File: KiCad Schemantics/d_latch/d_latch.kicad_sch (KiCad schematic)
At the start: 5 parts

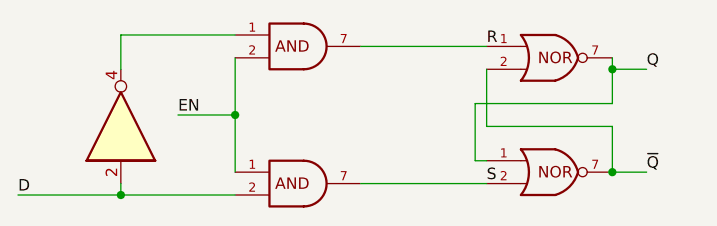
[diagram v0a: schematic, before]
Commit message: DrawIo Diagrams for the D Latch
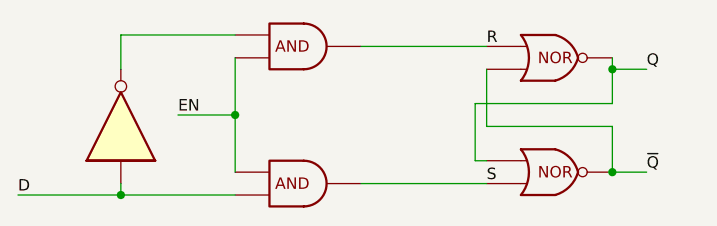
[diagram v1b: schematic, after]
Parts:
- U? (x2): value 74AUC2G08 -> (none)
- U? (x2): value 74AUC2G02 -> (none)
- U?: value 74LVC1GU04DRL -> (none); footprint Package_TO_SOT_SMD:SOT-553 -> (none)
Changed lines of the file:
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@@
     (effects (font (size 1.27 1.27)) (justify left bottom))
   )
-  (symbol (lib_id "74xGxx:74AUC2G08") (at 106.68 60.96 0) (unit 1)
+  (symbol (lib_name "74AUC2G08_1") (lib_id "74xGxx:74AUC2G08") (at 106.68 60.96 0) (unit 1)
     (in_bom yes) (on_board yes) (fields_autoplaced)
     (property "Reference" "U?" (id 0) (at 106.045 53.34 0)
       (effects (font (size 1.27 1.27)) hide)
     )
-    (property "Value" "74AUC2G08" (id 1) (at 106.045 55.88 0)
+    (property "Value" "" (id 1) (at 106.045 55.88 0)
       (effects (font (size 1.27 1.27)) hide)
     )
@@
       (effects (font (size 1.27 1.27)) hide)
     )
-    (property "Value" "74AUC2G08" (id 1) (at 106.045 71.12 0)
+    (property "Value" "" (id 1) (at 106.045 71.12 0)
       (effects (font (size 1.27 1.27)) hide)
     )
@@
       (effects (font (size 1.27 1.27)) hide)
     )
-    (property "Value" "74AUC2G02" (id 1) (at 133.985 69.85 0)
+    (property "Value" "" (id 1) (at 133.985 69.85 0)
       (effects (font (size 1.27 1.27)) hide)
     )
@@
       (effects (font (size 1.27 1.27)) hide)
     )
-    (property "Value" "74LVC1GU04DRL" (id 1) (at 85.0392 58.42 90)
+    (property "Value" "" (id 1) (at 85.0392 58.42 90)
       (effects (font (size 1.27 1.27)) hide)
     )
-    (property "Footprint" "Package_TO_SOT_SMD:SOT-553" (id 2) (at 86.36 64.77 0)
+    (property "Footprint" "" (id 2) (at 86.36 64.77 0)
       (effects (font (size 1.27 1.27)) hide)
     )
@@
     (pin "4")
   )
-  (symbol (lib_id "74xGxx:74AUC2G02") (at 134.62 62.23 0) (unit 1)
+  (symbol (lib_name "74AUC2G02_1") (lib_id "74xGxx:74AUC2G02") (at 134.62 62.23 0) (unit 1)
     (in_bom yes) (on_board yes) (fields_autoplaced)
     (property "Reference" "U?" (id 0) (at 133.985 54.61 0)
       (effects (font (size 1.27 1.27)) hide)
     )
-    (property "Value" "74AUC2G02" (id 1) (at 133.985 57.15 0)
+    (property "Value" "" (id 1) (at 133.985 57.15 0)
       (effects (font (size 1.27 1.27)) hide)
     )
